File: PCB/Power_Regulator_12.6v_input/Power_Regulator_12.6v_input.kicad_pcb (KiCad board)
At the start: 2 copper layers, 90 x 90 mm, 65 parts, among them J1 SE2-30, J10 Conn_01x01_Pin, J12 Conn_01x01_Pin, J13 Conn_01x01_Pin, J2 Jack-DC, J3 Conn_01x05_Pin, J4 Conn_01x01_Pin, J5 Conn_01x01_Pin, J6 Conn_01x01_Pin, J7 Conn_01x01_Pin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

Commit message: edits from meeting
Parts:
- +Batt 24v: renamed from J9
- +Batt 5v: renamed from J8
- 24V pre Relay: renamed from J6
- 3.3 relay logic input: renamed from J13
- 3.3V out: renamed from J5
- 5v in to 3.3: renamed from J10
- Relay Logic: renamed from J12
- moved J3 17.7 mm to (161.1, 115.3)
- renumbered J7 to +24v, J4 to +5V
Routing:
- net +BATT: track 162.7 -> 128.9 mm
- net /24V_RAW: track 87.8 -> 68.9 mm
- net +3.3VA: track 171.2 -> 160.5 mm
- net GND: vias 111 -> 109
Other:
- board size 90 x 90 mm -> 90 x 85 mm

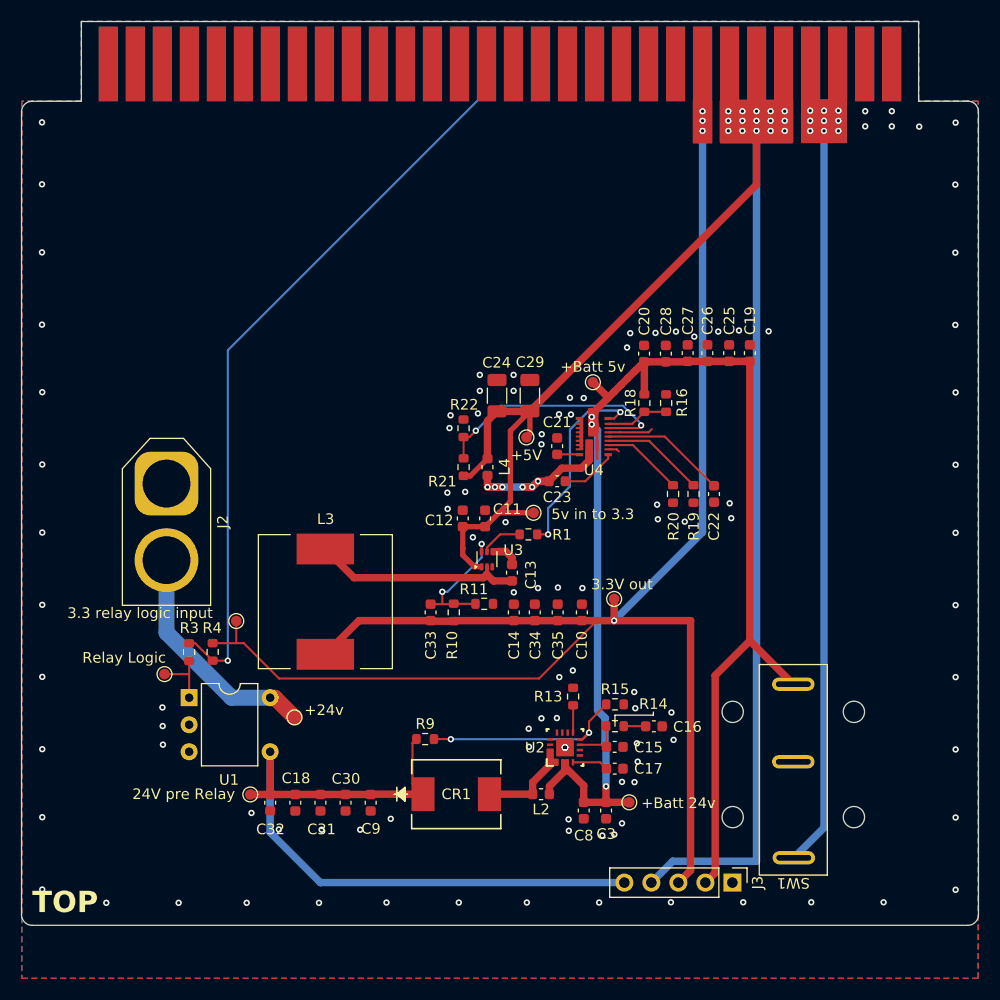
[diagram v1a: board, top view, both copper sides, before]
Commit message: updated board footprint and rerouted
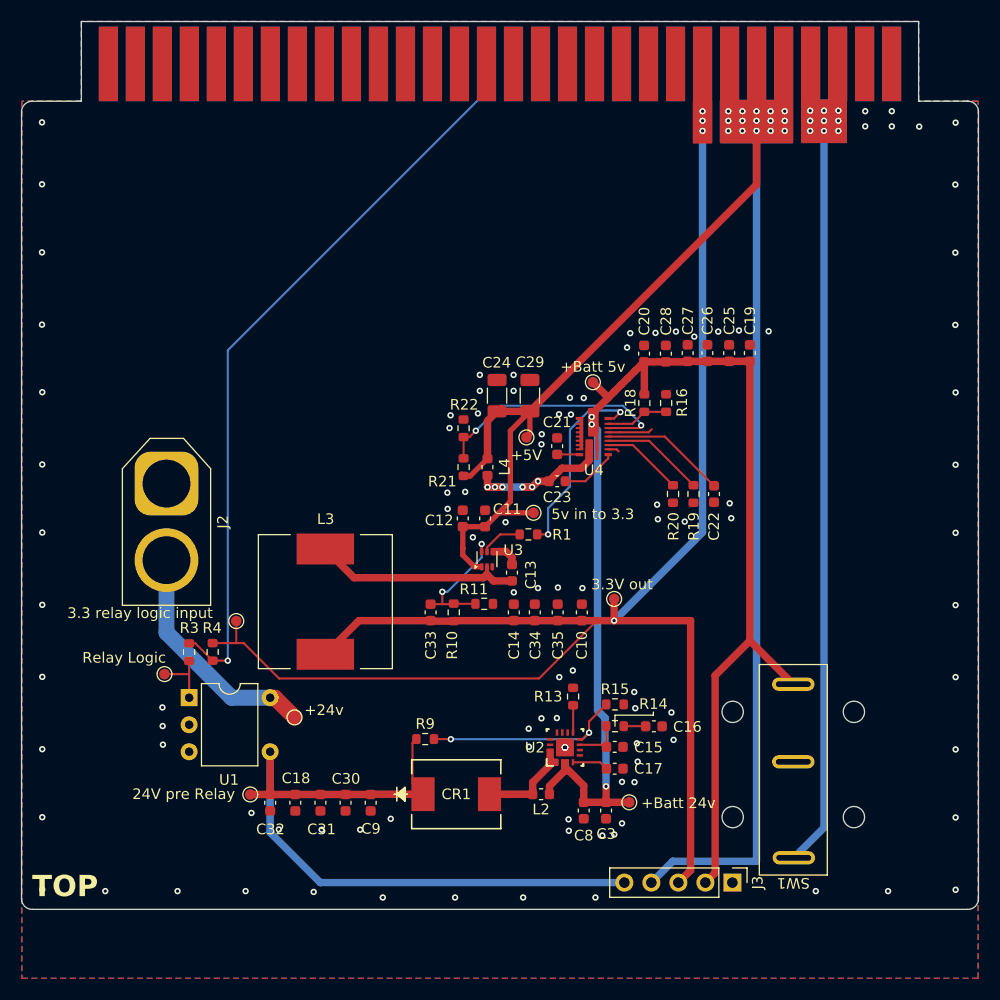
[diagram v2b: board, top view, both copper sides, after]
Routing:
- net GND: vias 109 -> 107
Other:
- board size 90 x 85 mm -> 90 x 83.5 mm
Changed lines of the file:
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@@
 		(fp_line
 			(start -45 4.5)
-			(end -45 80.01)
+			(end -45 78.5)
 			(stroke
 				(width 0.05)
@@
 		)
 		(fp_line
-			(start -44 81)
-			(end 44 81)
+			(start -44 79.5)
+			(end 44 79.5)
 			(stroke
 				(width 0.05)
@@
 		(fp_line
 			(start 45 4.49)
-			(end 45 80)
+			(end 45 78.5)
 			(stroke
 				(width 0.05)
@@
 		)
 		(fp_arc
-			(start -44 81)
-			(mid -44.707107 80.707107)
-			(end -45 80)
+			(start -44 79.5)
+			(mid -44.707107 79.207107)
+			(end -45 78.5)
 			(stroke
 				(width 0.05)
@@
 		)
 		(fp_arc
-			(start 45 80)
-			(mid 44.707107 80.707107)
-			(end 44 81)
+			(start 45 78.5)
+			(mid 44.707107 79.207107)
+			(end 44 79.5)
 			(stroke
 				(width 0.05)
@@
 		)
 		(fp_text user "TOP"
-			(at -44 80 0)
+			(at -44 78.5 0)
 			(unlocked yes)
 			(layer "F.SilkS")
@@
 		)
 		(fp_text user "BOTTOM"
-			(at -44 80 0)
+			(at -44 78.5 0)
 			(unlocked yes)
 			(layer "B.SilkS")
@@
 			(layer "Cmts.User")
 			(pts
-				(xy 184.275 119.815) (xy 183.982107 41.815)
+				(xy 184.275 117.815) (xy 183.982107 41.815)
 			)
 			(height 11.5)
@@
 				(keep_text_aligned yes)
 			)
-			(gr_text "78"
-				(at 194.625 80.815 90)
+			(gr_text "76"
+				(at 194.625 79.815 90)
 				(layer "Cmts.User")
 				(effects
@@
 			(layer "Cmts.User")
 			(pts
-				(xy 189.275 119.815) (xy 188.982107 34.315)
+				(xy 178.645 34.315) (xy 178.645 41.805)
 			)
-			(height 11.5)
+			(height 9.63)
 			(orientation 1)
 			(format
@@
 			)
 			(style
-				(thickness 0.05)
+				(thickness 0.1)
 				(arrow_length 1.27)
 				(text_position_mode 0)
@@
 				(keep_text_aligned yes)
 			)
-			(gr_text "85.5"
-				(at 199.625 77.065 90)
+			(gr_text "7.49"
+				(at 187.175 38.06 90)
 				(layer "Cmts.User")
 				(effects
 					(font
 						(size 1 1)
-						(thickness 0.15)
+						(thickness 0.1)
 					)
 				)
@@
 			(layer "Cmts.User")
 			(pts
-				(xy 94.275 119.315) (xy 184.275 119.315)
+				(xy 99.905 34.315) (xy 178.645 34.315)
 			)
-			(height 12)
+			(height -10.5)
 			(orientation 0)
 			(format
@@
 			)
 			(style
-				(thickness 0.05)
+				(thickness 0.1)
 				(arrow_length 1.27)
 				(text_position_mode 0)
@@
 				(keep_text_aligned yes)
 			)
-			(gr_text "90"
-				(at 139.275 130.165 0)
+			(gr_text "78.74"
+				(at 139.275 22.715 0)
 				(layer "Cmts.User")
 				(effects
 					(font
 						(size 1 1)
-						(thickness 0.15)
+						(thickness 0.1)
 					)
 				)
@@
 			(layer "Cmts.User")
 			(pts
-				(xy 99.905 34.315) (xy 178.645 34.315)
+				(xy 94.275 117.815) (xy 184.275 117.815)
 			)
-			(height -10.5)
+			(height 12)
 			(orientation 0)
 			(format
@@
 			)
 			(style
-				(thickness 0.1)
+				(thickness 0.05)
 				(arrow_length 1.27)
 				(text_position_mode 0)
@@
 				(keep_text_aligned yes)
 			)
-			(gr_text "78.74"
-				(at 139.275 22.715 0)
+			(gr_text "90"
+				(at 139.275 128.665 0)
 				(layer "Cmts.User")
 				(effects
 					(font
 						(size 1 1)
-						(thickness 0.1)
+						(thickness 0.15)
 					)
 				)
@@
 			(layer "Cmts.User")
 			(pts
-				(xy 178.645 34.315) (xy 178.645 41.805)
+				(xy 189.275 117.815) (xy 188.982107 34.315)
 			)
-			(height 9.63)
+			(height 11.5)
 			(orientation 1)
 			(format
@@
 			)
 			(style
-				(thickness 0.1)
+				(thickness 0.05)
 				(arrow_length 1.27)
 				(text_position_mode 0)
@@
 				(keep_text_aligned yes)
 			)
-			(gr_text "7.49"
-				(at 187.175 38.06 90)
+			(gr_text "83.5"
+				(at 199.625 76.065 90)
 				(layer "Cmts.User")
 				(effects
 					(font
 						(size 1 1)
-						(thickness 0.1)
+						(thickness 0.15)
 					)
 				)
@@
 		)
 		(group ""
-			(members "1165f2b9-ad39-46db-9355-2622baf5f341" "1a10eee6-b7c3-402c-8187-059c8d6060c5"
-				"29773198-3a98-4840-a3af-a3ca2cd658c5" "363fe6f3-add8-44af-a6e9-e83585f8e0e6"
-				"3ab83fb6-328b-4aad-9cfe-ea71da5e2e7b" "3ff6b9b7-9b22-425f-883b-d01962021f29"
-				"40969704-7888-45bf-ab7a-a53bec2bff01" "44bac66c-1010-4cd6-a9e4-1c2dea7179f5"
-				"45dc9cf5-1174-4060-8e36-baf8a2da95bc" "4c74b5c8-aa70-4270-8913-f7949eca2170"
-				"5608e8ac-3596-474f-b176-e6e41a1cf140" "6695a0fd-109c-474f-89a3-8a61135de04f"
-				"684056d5-9ce3-46cb-99b5-340d30f8f539" "6983dbd3-f4ac-4d42-b3e2-57c0dcc39f60"
-				"75f9f9a7-ee7e-4f9f-ab34-afefe529b8ee" "9665e481-cc1f-46c0-8b12-d23a6d129ef6"
-				"986d3e38-a9b8-4ad9-b3eb-4ff6d232fc49" "9e06b457-9fde-455f-af6d-39ec3d68c539"
-				"a2b7cc0b-e9d5-412b-be57-aa380d5e3ed9" "ac8badf1-bce6-4a8a-81eb-bd84dbf5379e"
-				"b2ba81e0-b005-4e5c-820d-60ec21c67bda" "b669fce2-e880-4914-a0a3-2b0b4b3f7b29"
-				"c8e9be68-783d-4d57-b17d-960176c05508" "c9403f78-07e7-4458-add2-b21b336ea91e"
-				"da48b122-58a5-4282-bf96-9f909cb217dc" "da645934-a3e4-4388-9207-35ec8d2ad102"
-				"ea7c78ff-0247-4067-8d1d-cafc605e2531" "edcd813a-ff3c-443c-b242-db4c4cae5229"
-				"f1ae07b9-9dbd-4294-9a9e-c6f43ac08833" "f5dde6bf-69eb-4599-b331-30237cfba745"
-				"fafab35a-7dfc-459d-9129-1ed883ab2993"
+			(members "1258a9b6-a472-40f8-88e8-61c6a7f54d30" "1310b3cc-6ccb-4bc7-812d-13a53c35bede"
+				"13256619-bb74-43bd-9704-3dd4d63f77fd" "13f5031e-444a-4e07-a34c-dcf9f83d3cd4"
+				"1940ba9b-5398-493c-8630-c6868596514e" "1e50864e-45a4-496d-a7ce-a668c990ccb3"
+				"29528cd6-9d67-4d20-b8ac-7de1f08a8ae9" "2f465589-3dfc-4345-aa36-fca926126d9f"
+				"2fb64ac3-e25a-462f-b1e9-bcbd3f4f3d70" "353f7f56-ffd0-4264-a075-44ce0ea350a2"
+				"395a9683-0763-486c-b877-66918c7dc31b" "501c2c12-8468-4884-9879-e5bd5ef62d80"
+				"5f6c6a76-0e94-4ee7-9759-e59daa1b6cd5" "629a293d-5c29-4189-8a34-3a7cdaac2298"
+				"66c852fa-ccd0-49c7-95b2-9c1dfd5f89ef" "72b0e19b-bb28-443d-9416-65e7d09f8403"
+				"7ca9422a-6b5e-4c0c-9f6c-d7489bd05437" "8ef91ecc-6b82-4c12-b257-1344979eb3c9"
+				"8fa8e124-8042-4575-8b91-c9245a2853f0" "9eb8efc2-a171-4e15-a897-185d890ef4ed"
+				"a409d2f2-be99-47ed-b47b-98c75f3fc653" "b350c62a-9746-40c7-a2bf-b73dc40b1034"
+				"b9a70584-df6c-4f26-af10-f57b5a90d070" "bd25b185-b20f-4791-b129-52f502f4730c"
+				"c0aae9b7-97e4-4e7b-bd63-7a65869d4a4b" "c11ebc01-c09c-4a1d-8e9e-31e4d2e572bf"
+				"c5ac67a6-f6ce-4b66-9600-89c2a656a88e" "d3f7748e-5edf-40a0-9cb8-a1dac257c4ef"
+				"d97ae7b9-b4af-4102-9754-d03a398a146b" "f4cc148d-85d7-4531-89c4-40d25a14d757"
+				"f9f0d38b-911f-456f-9b49-91f4f0753dff"
 			)
 		)
 		(group ""
-			(members "5233c64e-c49d-4780-801c-84ff527a4543" "71493117-279e-4f09-8949-e8f5d8b40db2"
-				"aa828052-4307-46b1-9b4e-2e158c113866" "b87645be-9a32-46e4-832b-78a4c8476af4"
-				"f29ece7c-eaca-452a-8fcf-1d41fddeeeba" "f2ace002-c458-4d03-a636-8fbf77f32291"
+			(members "00be4426-2798-4f5d-83c9-b3e2dcae1432" "197e8c2e-cc9d-490a-ba47-6393226a3647"
+				"742c247a-c85b-420f-a4f2-0a5ea8414580" "907916e9-5d62-4696-9eb8-ab0391d74d71"
+				"95efff6f-719b-4fa0-ae27-666eac963d57" "e7ef485f-69d9-4f2b-97ce-225cd0003b7a"
 			)
 		)
@@
 	)
 	(via
-		(at 128.6 117.175)
+		(at 128.25 116.7)
 		(size 0.6)
 		(drill 0.3)
@@
 	)
 	(via
-		(at 135.4 117.175)
+		(at 135.05 116.7)
 		(size 0.6)
 		(drill 0.3)
@@
 	)
 	(via
-		(at 148.6 117.175)
+		(at 148.25 116.7)
 		(size 0.6)
 		(drill 0.3)
@@
 	)
 	(via
-		(at 102.25 117.2)
+		(at 102.15 116.1)
 		(size 0.6)
 		(drill 0.3)
@@
 	)
 	(via
-		(at 155.35 117.15)
-		(size 0.6)
-		(drill 0.3)
-		(layers "F.Cu" "B.Cu")
-		(free yes)
-		(net 2)
-	)
-	(via
 		(at 139.8 81.4)
 		(size 0.6)
@@
 	)
 	(via
-		(at 115.45 117.2)
+		(at 115.35 116.1)
 		(size 0.6)
 		(drill 0.3)
@@
 	)
 	(via
-		(at 162.15 117.15)
-		(size 0.6)
-		(drill 0.3)
-		(layers "F.Cu" "B.Cu")
-		(free yes)
-		(net 2)
-	)
-	(via
 		(at 134.525 72.55)
 		(size 0.6)
@@
 	)
 	(via
-		(at 122.25 117.2)
+		(at 121.75 116.175)
 		(size 0.6)
 		(drill 0.3)
@@
 	)
 	(via
-		(at 168.55 117.15)
+		(at 168.975 116.1)
 		(size 0.6)
 		(drill 0.3)
@@
 	)
 	(via
-		(at 141.8 117.175)
+		(at 141.45 116.7)
 		(size 0.6)
 		(drill 0.3)
@@
 	)
 	(via
-		(at 175.35 117.15)
+		(at 175.775 116.1)
 		(size 0.6)
 		(drill 0.3)
@@
 	)
 	(via
-		(at 109.05 117.2)
+		(at 108.95 116.1)
 		(size 0.6)
 		(drill 0.3)
